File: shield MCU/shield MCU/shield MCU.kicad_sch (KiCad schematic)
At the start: 16 parts, among them J1 IR_sensor, J2 IR_sensor, J3 IR_sensor, J4 IR_sensor, J5 IR_sensor

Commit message: Valmis schema
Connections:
- net at J4.1 (P1): now also U?.130 (PF3)
- net at J3.1 (P1): now also U?.37 (PC3)
- net at J2.1 (P1): now also U?.38 (PC0)
- net at U?.108 (PF5): now also J5.1 (P1)
- net at U?.109 (PA3): now also J1.1 (P1)
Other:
- moved on the sheet: J1, J2, J3, J4, J5, PoL?, U?

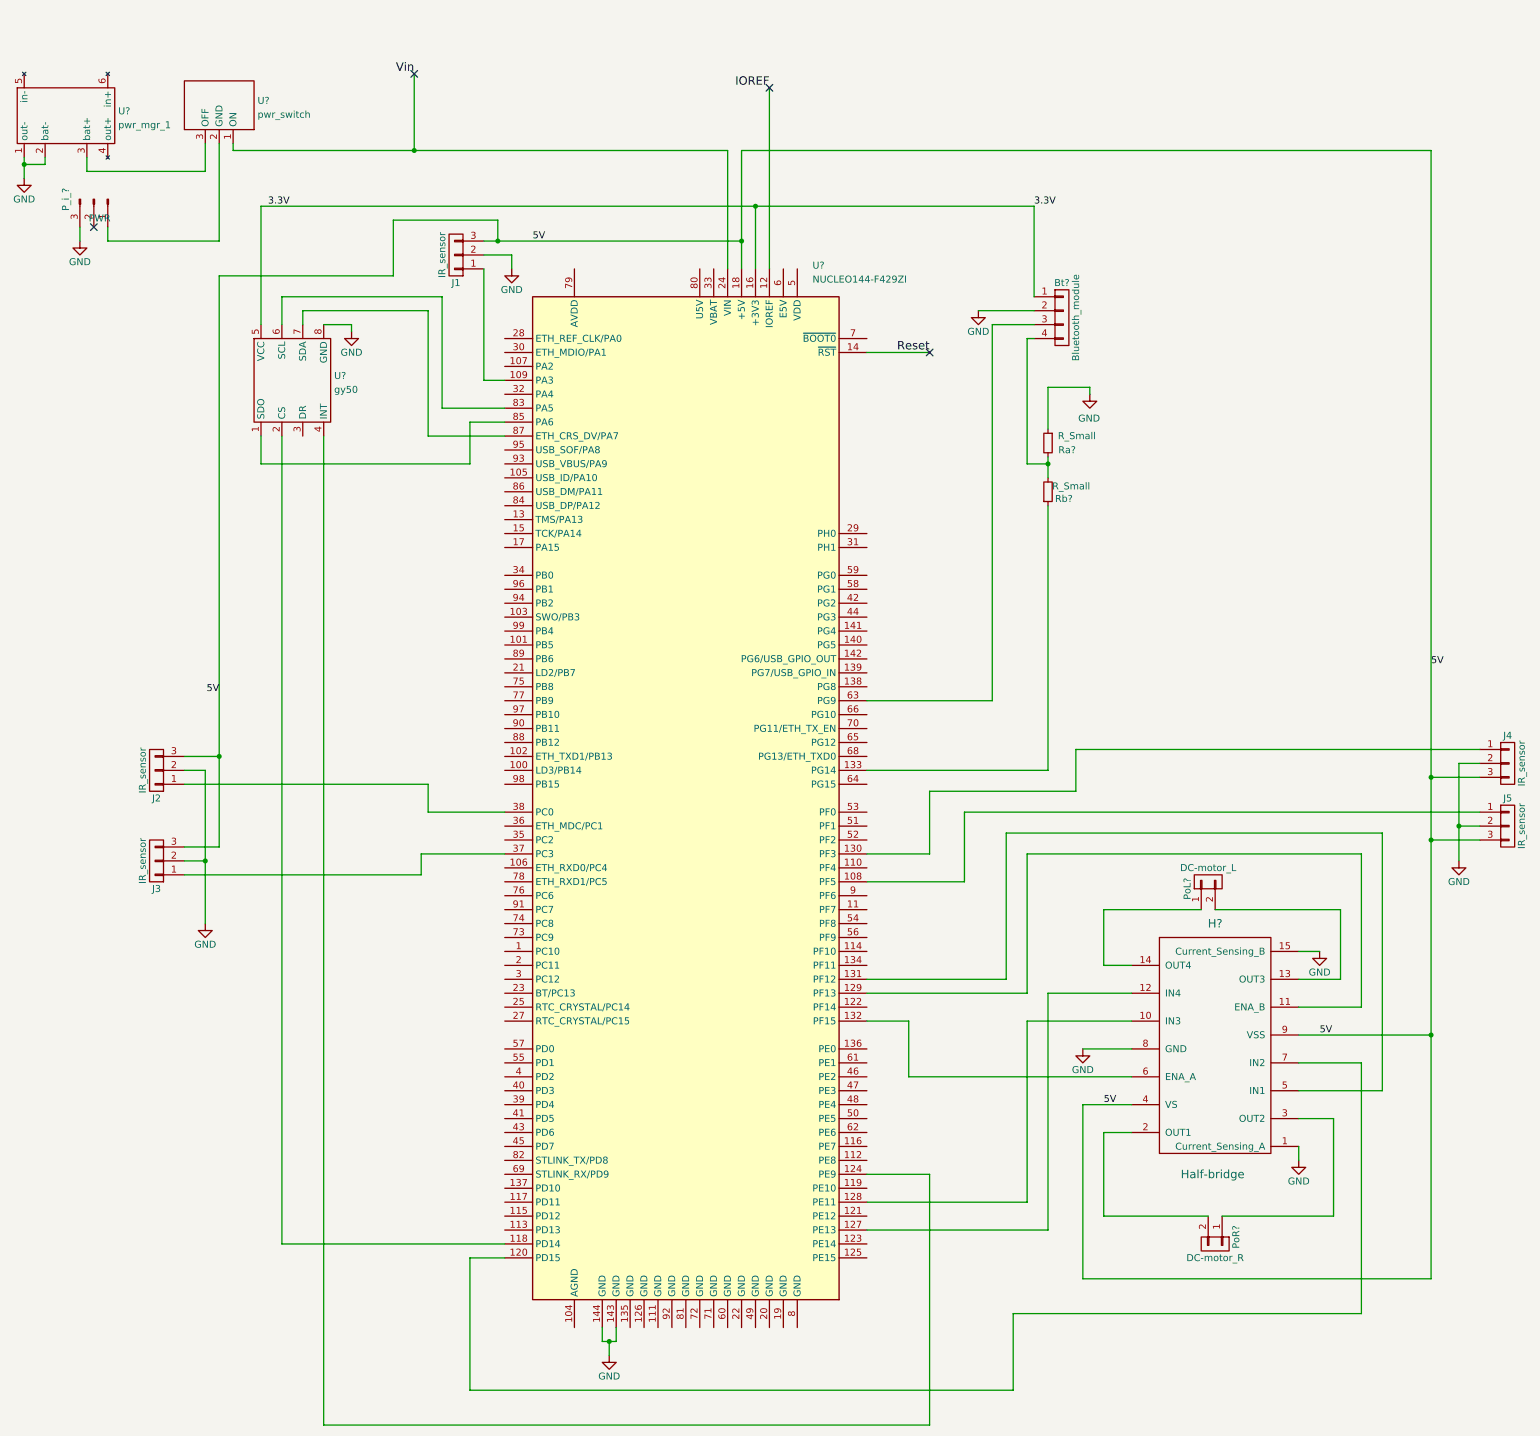
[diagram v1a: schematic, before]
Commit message: vetoja vaille valmis
Poistin kaikki käyttämättömät pinnit, koska helpottaa layouttia
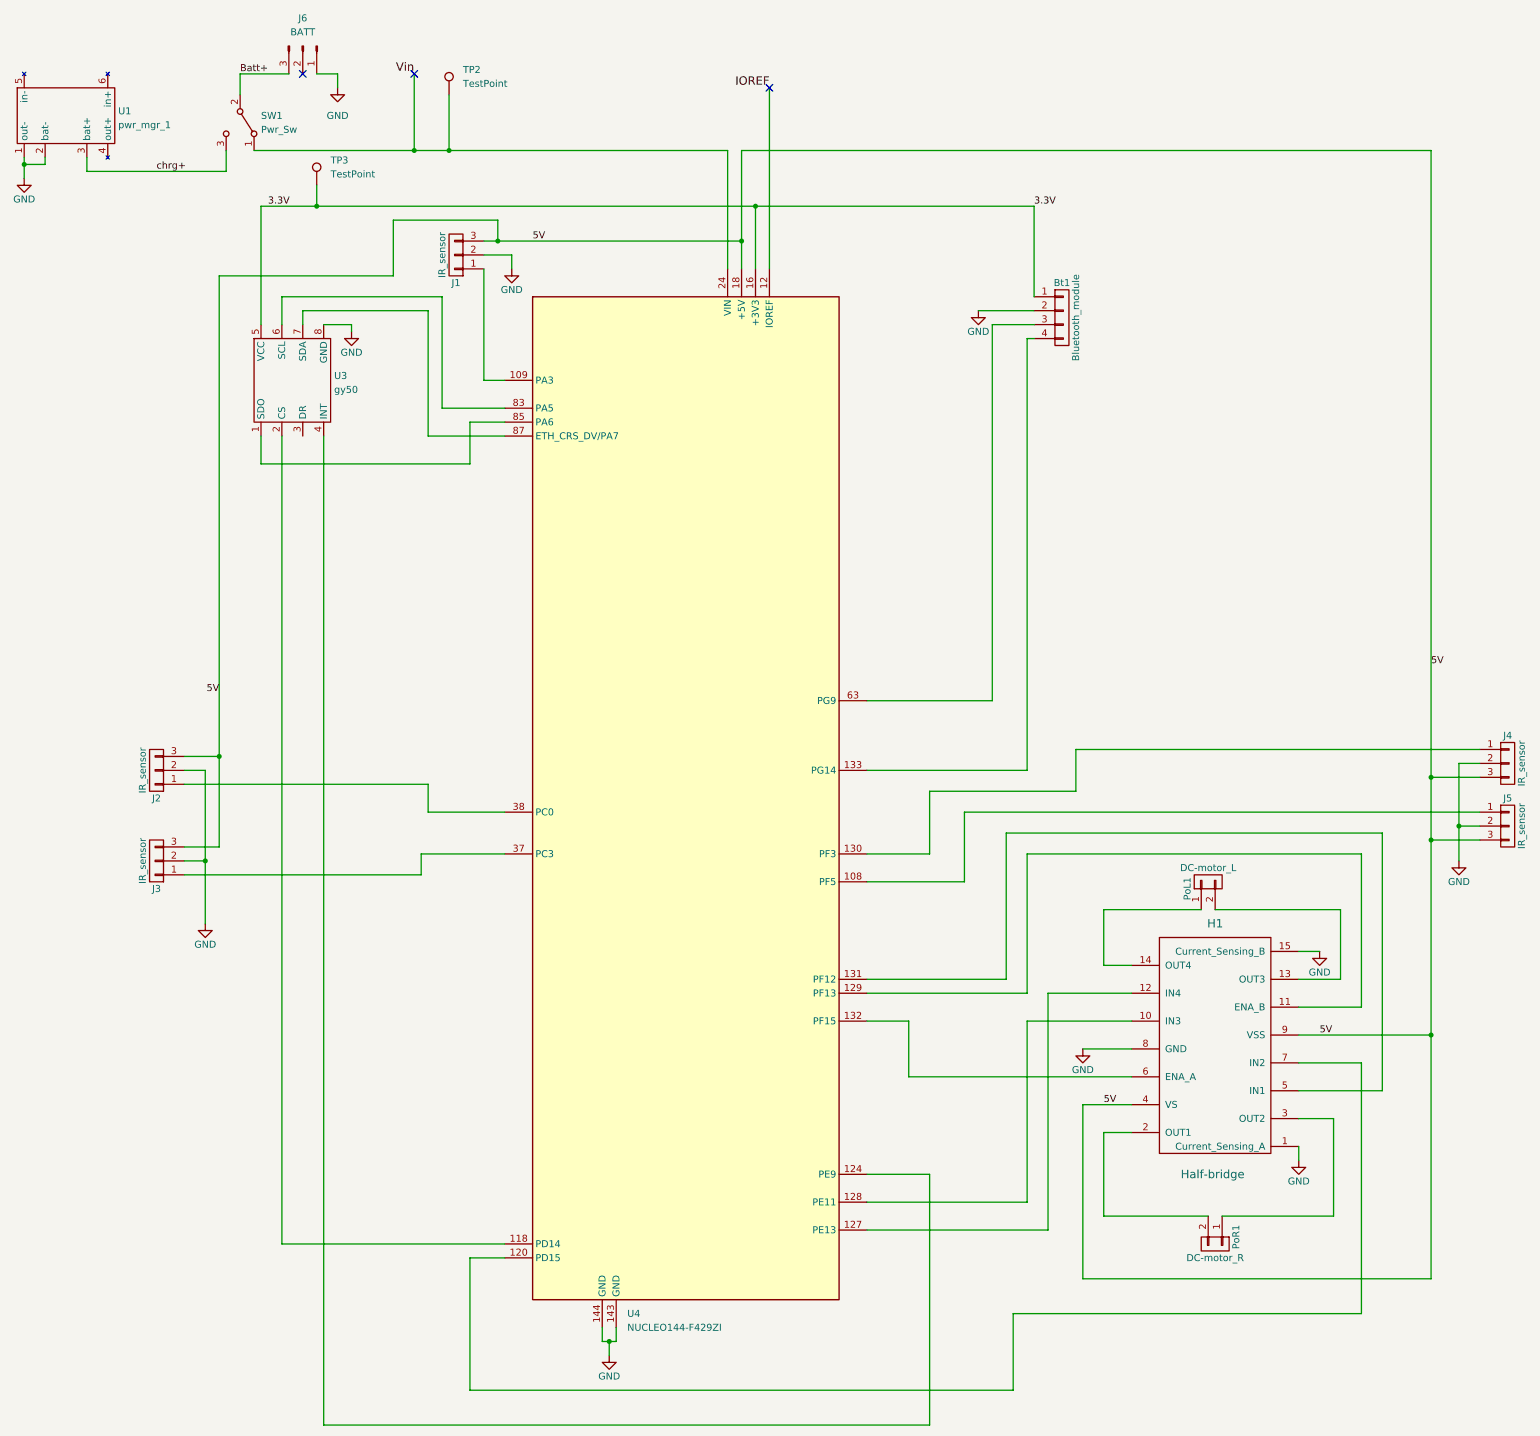
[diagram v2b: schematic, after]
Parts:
- removed P_i_?: PWR, Connector_PinHeader_2.54mm:PinHeader_1x03_P2.54mm_Horizontal, symbol Connector:Conn_01x03_Male
- removed Ra?, Rb?: R_Small, Connector_PinHeader_2.54mm:PinHeader_1x02_P2.54mm_Horizontal, symbol ardu_auto2_0-rescue:R_Small-Arduino_shield-rescue
- removed U?: pwr_switch, pwr_mgr:pwr_stw, symbol pwr_mgr:pwr_switch
- added J6: BATT, Omat:Connector_3pin, symbol Connector:Conn_01x03_Male
- added SW1: Pwr_Sw, Omat:SPDT, symbol Switch:SW_SPDT
- added TP2, TP3: TestPoint, Connector_Pin:Pin_D0.7mm_L6.5mm_W1.8mm_FlatFork, symbol Connector:TestPoint
- H1: renamed from H?; footprint Halfbrifge:Half-bridge -> Omat:L298HN
- U1: renamed from U?; footprint pwr_mgr:pwr_mfr_1 -> Omat:TPS4056
- U3: renamed from U?; footprint pwr_mgr:gy50 -> Omat:GY-50
- U4: renamed from U?; footprint Module:ST_Morpho_Connector_144_STLink_MountingHoles -> Omat:ST_Morpho_Connector_144_STLink_MountingHoles_modded
- gave numbers to parts that had none: 3
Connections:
- net 3.3V: now also TP3.1
- net GND: now also J6.1 (Pin_1)
- net Vin: now also SW1.1 (A), TP2.1
- net at U4.133 (PG14): now also Bt1.4 (P4)
- net chrg+: now reaches U1.3 (bat+)
- net chrg+: now also SW1.3 (C)
- removed net Reset: U4.14 (~{RST})
- new net Batt+: J6.3 (Pin_3), SW1.2 (B)
- no-connect marks 4 -> 3
